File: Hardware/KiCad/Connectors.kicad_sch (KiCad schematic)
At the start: 56 parts

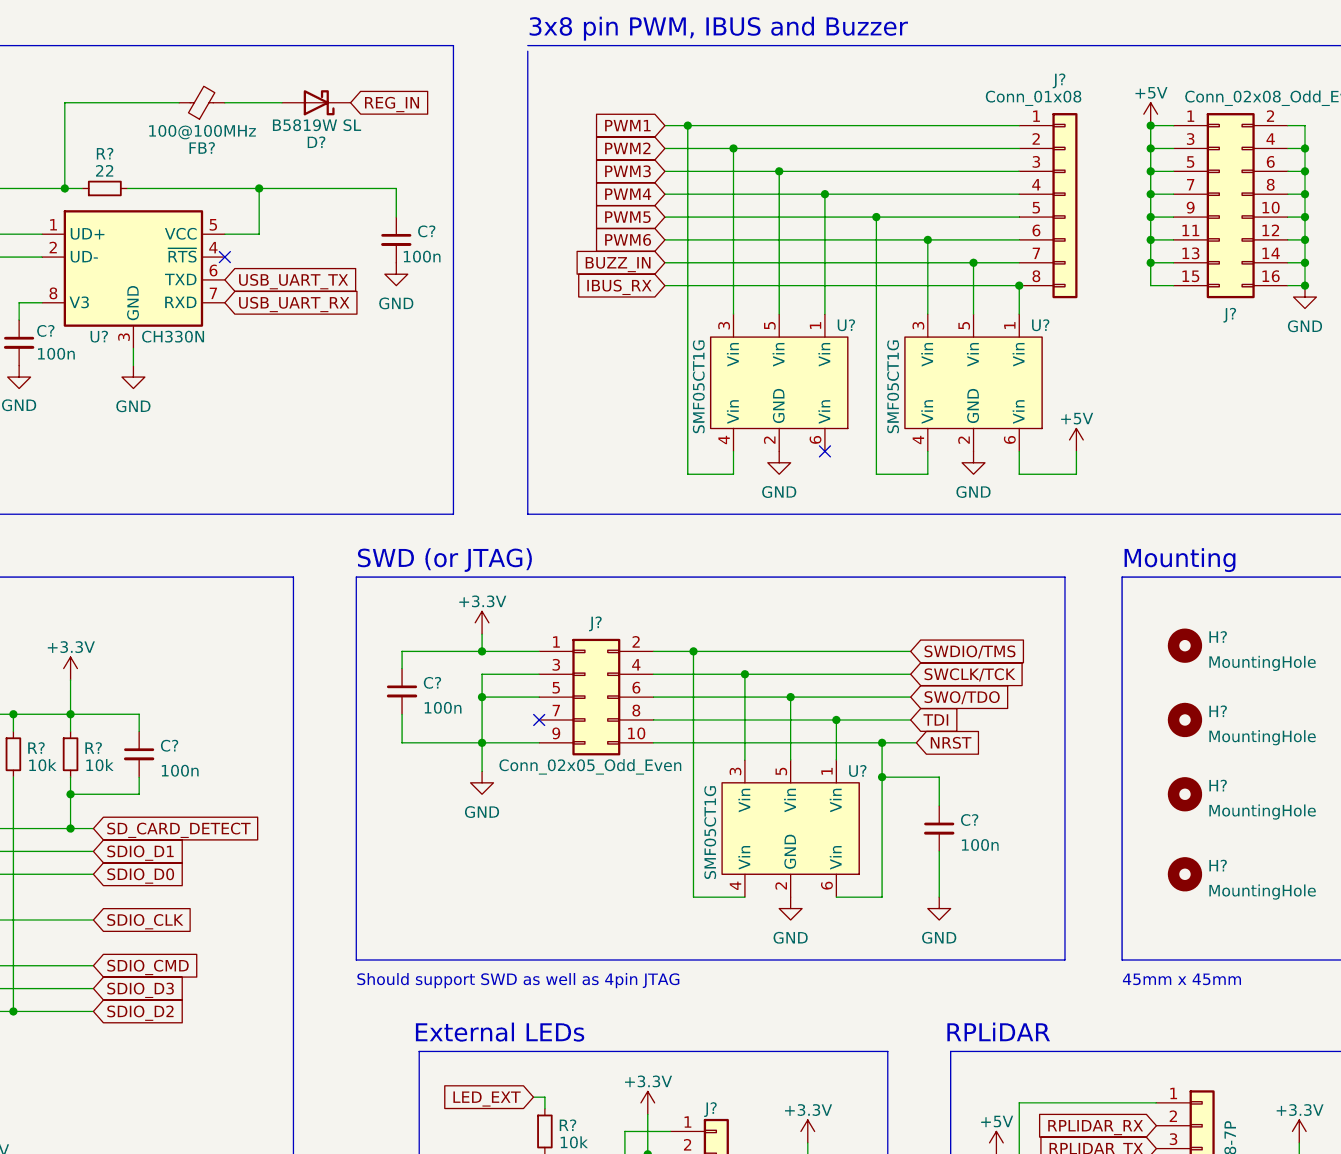
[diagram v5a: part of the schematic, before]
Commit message: Changed supply voltage for CH330N 5V->3V3
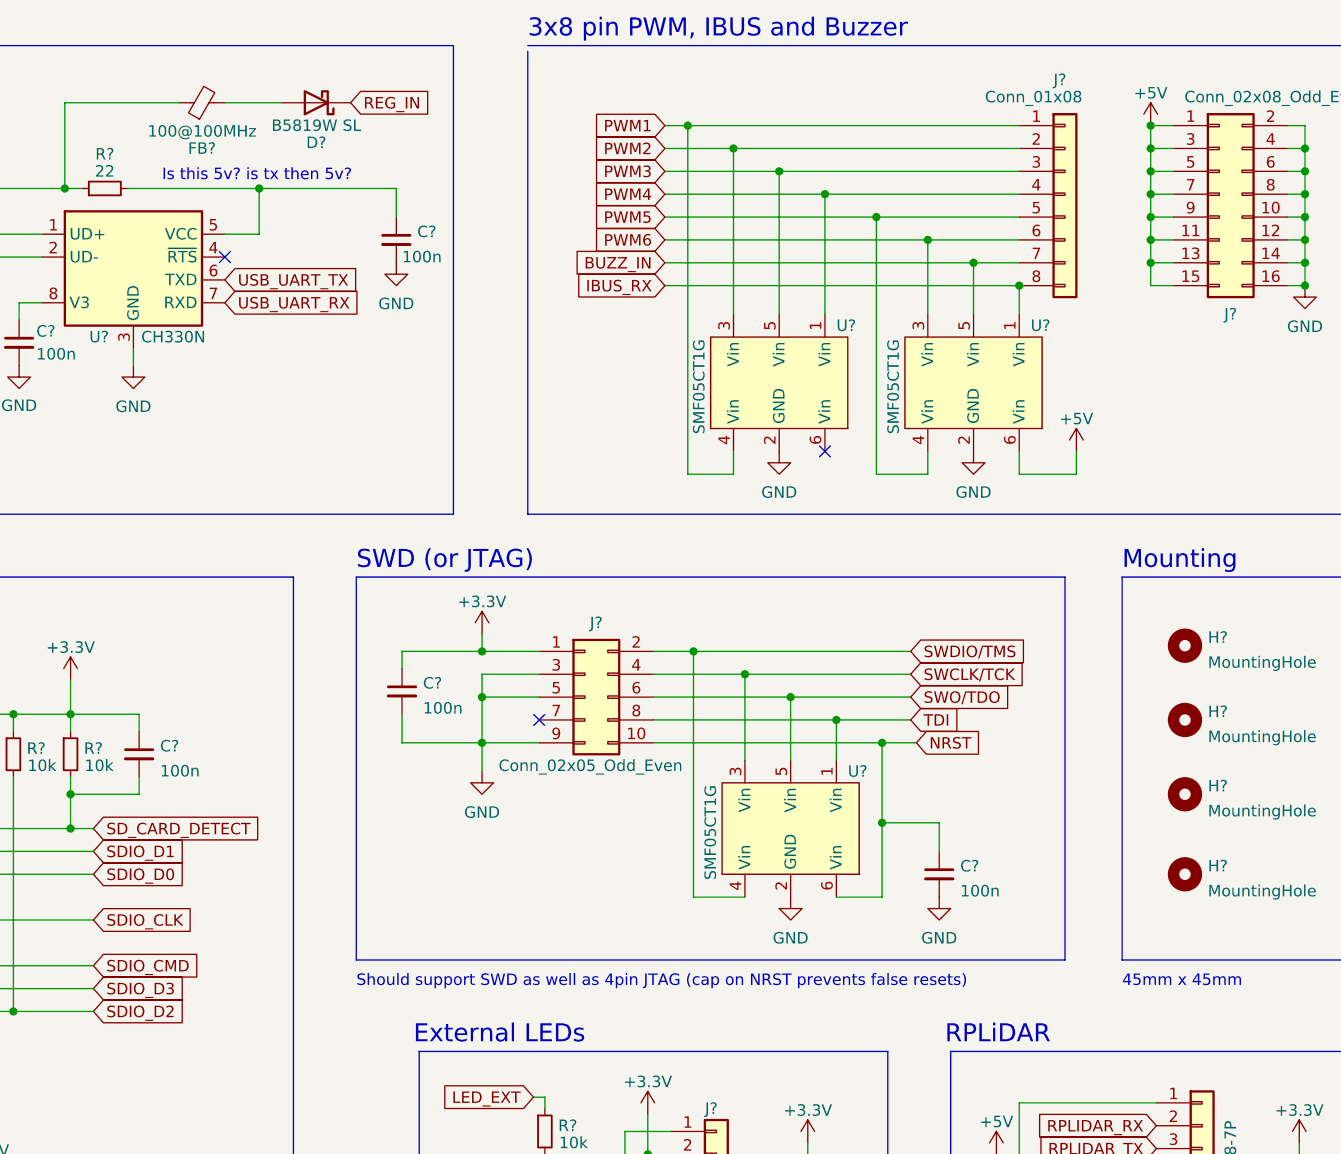
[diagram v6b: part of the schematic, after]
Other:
- note added: "Is this 5v? is tx then 5v?"
- note added: "Should support SWD as well as 4pin JTAG (cap on NRST prevents false resets)"
- note removed: "Should support SWD as well as 4pin JTAG"
- moved on the sheet: C?
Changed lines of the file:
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@@
   (junction (at 49.53 85.09) (diameter 0) (color 0 0 0 0)
   )
+  (junction (at 222.25 105.41) (diameter 0) (color 0 0 0 0)
+  )
   (junction (at 201.295 86.36) (diameter 0) (color 0 0 0 0)
   )
@@
   )
   (junction (at 125.73 126.365) (diameter 0) (color 0 0 0 0)
-  )
-  (junction (at 222.25 100.33) (diameter 0) (color 0 0 0 0)
   )
   (junction (at 104.14 173.355) (diameter 0) (color 0 0 0 0)
@@
     (stroke (width 0) (type default) (color 0 0 0 0))
   )
-  (wire (pts (xy 228.6 100.33) (xy 222.25 100.33))
+  (wire (pts (xy 228.6 105.41) (xy 222.25 105.41))
     (stroke (width 0) (type default) (color 0 0 0 0))
   )
@@
     (stroke (width 0) (type default) (color 0 0 0 0))
   )
+  (wire (pts (xy 222.25 105.41) (xy 222.25 113.665))
+    (stroke (width 0) (type default) (color 0 0 0 0))
+  )
   (wire (pts (xy 269.24 33.02) (xy 269.24 30.48))
     (stroke (width 0) (type default) (color 0 0 0 0))
@@
     (stroke (width 0) (type default) (color 0 0 0 0))
   )
-  (wire (pts (xy 228.6 103.505) (xy 228.6 100.33))
+  (wire (pts (xy 228.6 108.585) (xy 228.6 105.41))
     (stroke (width 0) (type default) (color 0 0 0 0))
   )
@@
     (stroke (width 0) (type default) (color 0 0 0 0))
   )
-  (wire (pts (xy 228.6 108.585) (xy 228.6 113.665))
-    (stroke (width 0) (type default) (color 0 0 0 0))
-  )
   (wire (pts (xy 31.115 40.005) (xy 44.45 40.005))
     (stroke (width 0) (type default) (color 0 0 0 0))
@@
     (stroke (width 0) (type default) (color 0 0 0 0))
   )
-  (wire (pts (xy 222.25 96.52) (xy 222.25 100.33))
-    (stroke (width 0) (type default) (color 0 0 0 0))
-  )
   (wire (pts (xy 99.695 95.25) (xy 99.695 93.345))
     (stroke (width 0) (type default) (color 0 0 0 0))
@@
     (stroke (width 0) (type default) (color 0 0 0 0))
   )
-  (wire (pts (xy 222.25 100.33) (xy 222.25 113.665))
+  (wire (pts (xy 222.25 96.52) (xy 222.25 105.41))
     (stroke (width 0) (type default) (color 0 0 0 0))
   )
@@
     (effects (font (size 1.27 1.27)) (justify left bottom))
   )
+  (text "Is this 5v? is tx then 5v?" (at 142.24 34.29 0)
+    (effects (font (size 1.27 1.27)) (justify left bottom))
+  )
   (text "I2C external 1" (at 21.59 188.595 0)
     (effects (font (size 1.27 1.27)) (justify left bottom))
@@
     (effects (font (size 1.27 1.27)) (justify left bottom))
   )
-  (text "Should support SWD as well as 4pin JTAG" (at 163.83 123.825 0)
+  (text "Should support SWD as well as 4pin JTAG (cap on NRST prevents false resets)"
+    (at 163.83 123.825 0)
     (effects (font (size 1.27 1.27)) (justify left bottom))
   )
@@
     (pin "1")
   )
-  (symbol (lib_id "Device:C_Small") (at 228.6 106.045 0) (unit 1)
-    (in_bom yes) (on_board yes) (fields_autoplaced)
-    (property "Reference" "C?" (id 0) (at 230.9241 105.1428 0)
-      (effects (font (size 1.27 1.27)) (justify left))
-    )
-    (property "Value" "100n" (id 1) (at 230.9241 107.9179 0)
-      (effects (font (size 1.27 1.27)) (justify left))
-    )
-    (property "Footprint" "Capacitor_SMD:C_0402_1005Metric" (id 2) (at 228.6 106.045 0)
-      (effects (font (size 1.27 1.27)) hide)
-    )
-    (property "Datasheet" "~" (id 3) (at 228.6 106.045 0)
-      (effects (font (size 1.27 1.27)) hide)
-    )
+  (symbol (lib_id "Device:C_Small") (at 228.6 111.125 0) (unit 1)
+    (in_bom yes) (on_board yes) (fields_autoplaced)
+    (property "Reference" "C?" (id 0) (at 230.9241 110.2228 0)
+      (effects (font (size 1.27 1.27)) (justify left))
+    )
+    (property "Value" "100n" (id 1) (at 230.9241 112.9979 0)
+      (effects (font (size 1.27 1.27)) (justify left))
+    )
+    (property "Footprint" "Capacitor_SMD:C_0402_1005Metric" (id 2) (at 228.6 111.125 0)
+      (effects (font (size 1.27 1.27)) hide)
+    )
+    (property "Datasheet" "~" (id 3) (at 228.6 111.125 0)
+      (effects (font (size 1.27 1.27)) hide)
+    )

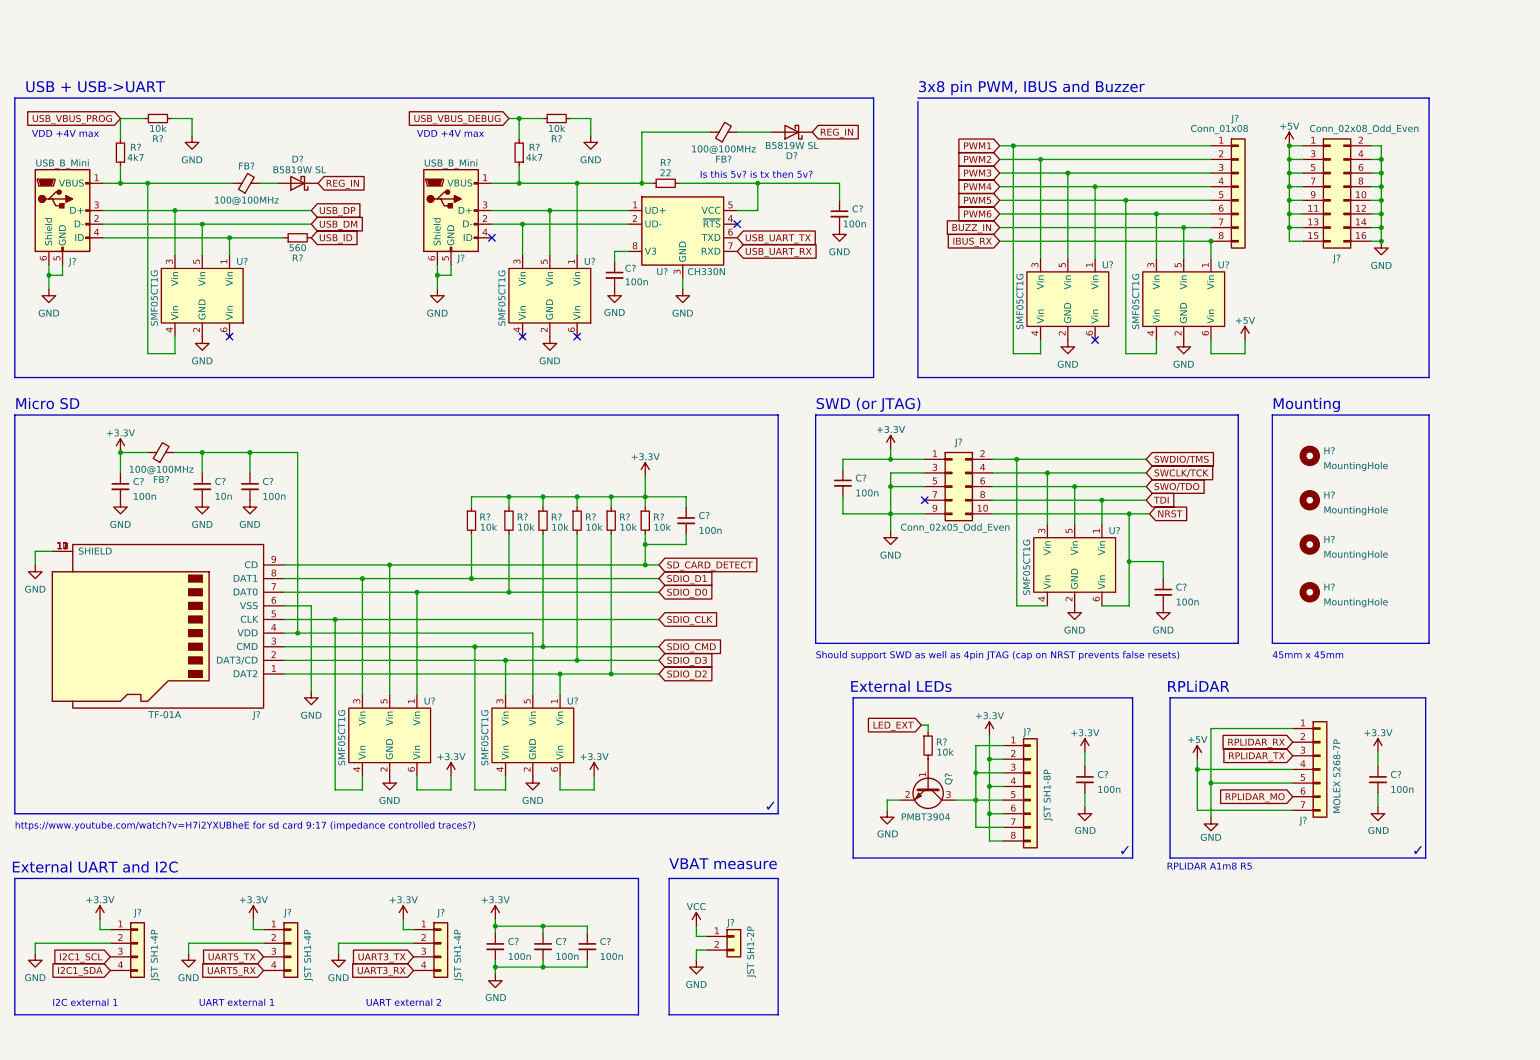
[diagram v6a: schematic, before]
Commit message: Added a missing connection between the BECs and the LDO, removed some duplicate ferrite bead filtering
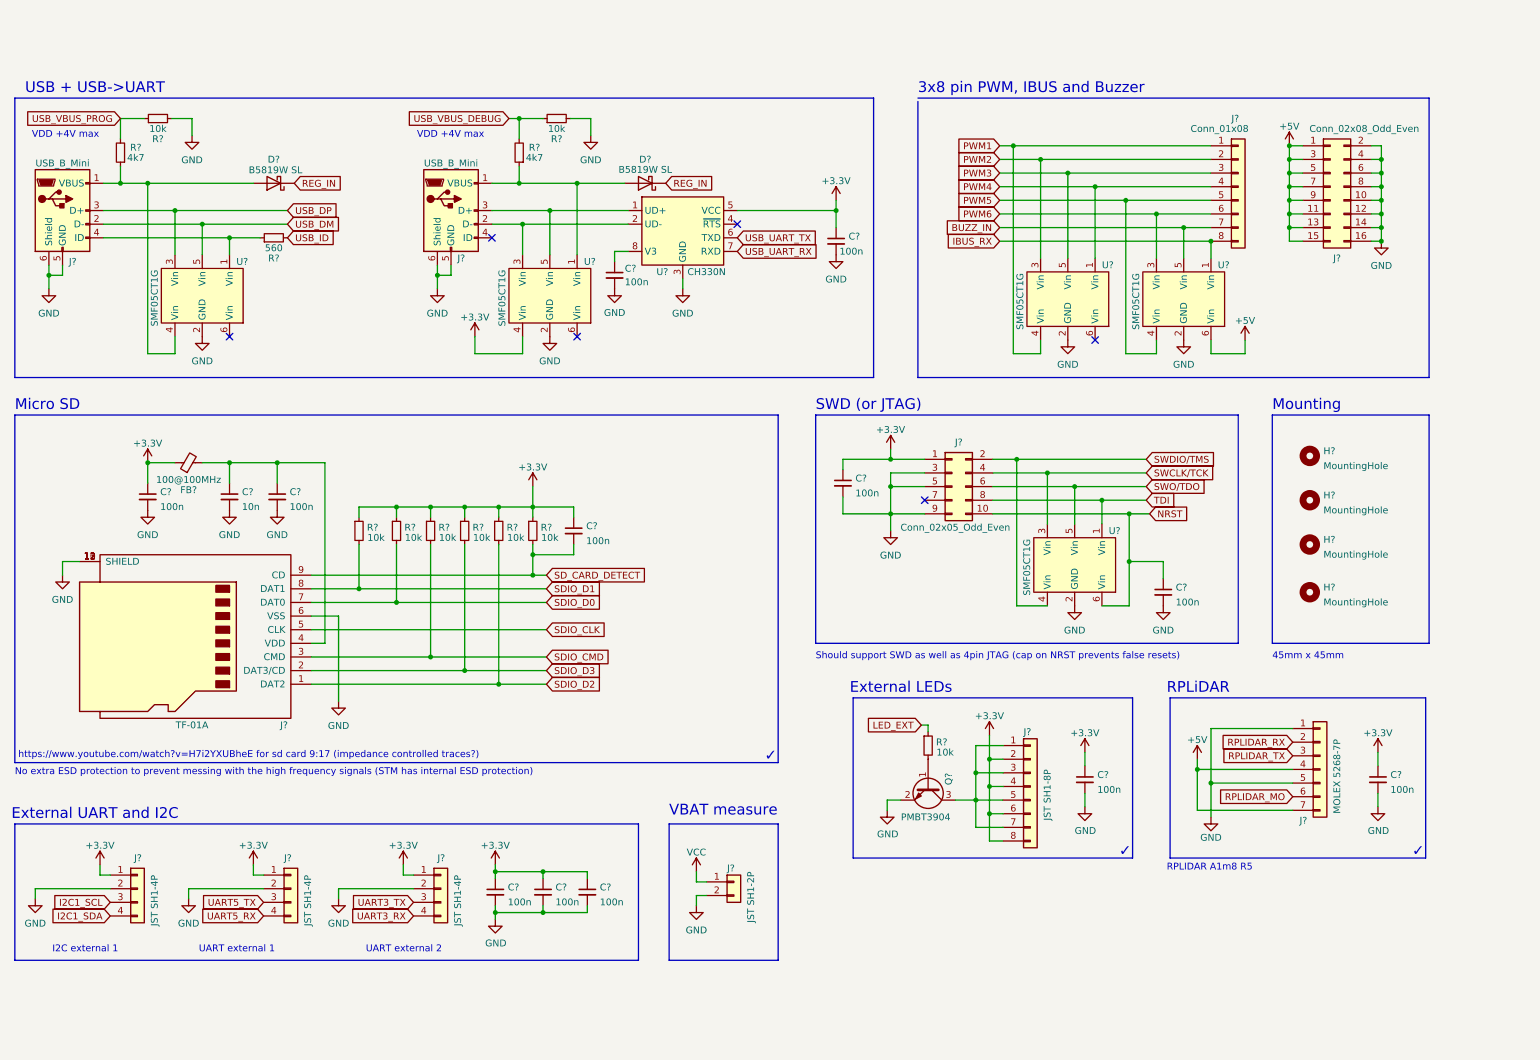
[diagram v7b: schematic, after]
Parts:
- removed FB? (x2): 100@100MHz, Inductor_SMD:L_0603_1608Metric, symbol Device:FerriteBead_Small
- removed R?: 22, Resistor_SMD:R_0402_1005Metric, symbol Device:R_Small
- removed U? (x2): SMF05CT1G, Package_TO_SOT_SMD:SOT-363_SC-70-6, symbol flightController:SMF05CT1G
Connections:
- net +3V3: now also C?.1, U?.4 (Vin), U?.5 (VCC)
- net at J?.1 (VBUS), R?.1, U?.1 (Vin): now also D?.2 (A)
- net at J?.1 (VBUS), R?.1, U?.4 (Vin): now also D?.2 (A)
- no-connect marks 7 -> 6
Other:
- note added: "No extra ESD protection to prevent messing with the high frequency signals (STM has internal ESD protection)"
- note removed: "Is this 5v? is tx then 5v?"
- moved on the sheet: C?, D?, FB?, J?, R?

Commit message: Added more filtering for the BMP, small labeling changes
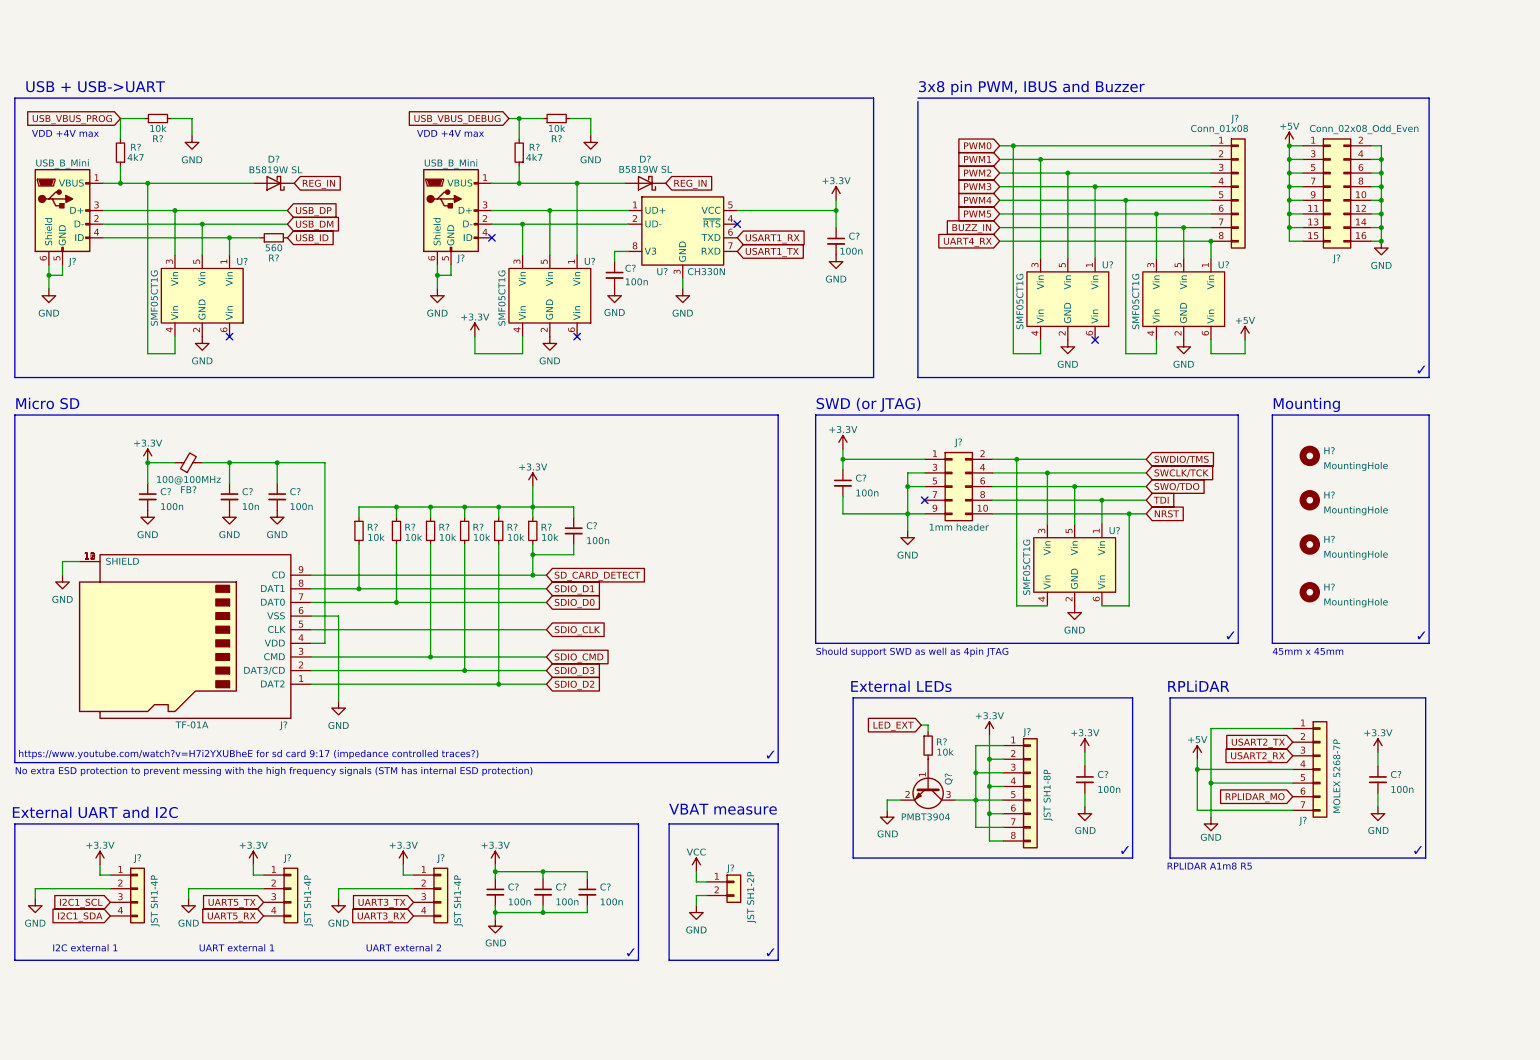
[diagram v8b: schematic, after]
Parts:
- removed C?: 100n, Capacitor_SMD:C_0402_1005Metric, symbol Device:C_Small
- J?: value Conn_02x05_Odd_Even -> 1mm header
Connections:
- net PWM6 is gone; now on net PWM5: J?.6 (Pin_6), U?.3 (Vin)
- net PWM1: now also J?.2 (Pin_2), U?.3 (Vin); no longer J?.1 (Pin_1), U?.4 (Vin)
- net PWM2: now also J?.3 (Pin_3), U?.5 (Vin); no longer J?.2 (Pin_2), U?.3 (Vin)
- net PWM3: now also J?.4 (Pin_4), U?.1 (Vin); no longer J?.3 (Pin_3), U?.5 (Vin)
- net PWM4: now also J?.5 (Pin_5), U?.4 (Vin); no longer J?.4 (Pin_4), U?.1 (Vin)
- net PWM5: no longer J?.5 (Pin_5), U?.4 (Vin)
- net IBUS_RX renamed UART4_RX
- net RPLIDAR_RX renamed USART2_TX
- net RPLIDAR_TX renamed USART2_RX
- net USB_UART_RX renamed USART1_TX
- net USB_UART_TX renamed USART1_RX
- new net PWM0: J?.1 (Pin_1), U?.4 (Vin)
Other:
- note added: "Should support SWD as well as 4pin JTAG"
- note removed: "Should support SWD as well as 4pin JTAG (cap on NRST prevents false resets)"
